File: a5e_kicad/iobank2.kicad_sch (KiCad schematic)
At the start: 2 parts, among them U7 A5EB013B-B23B

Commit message: Add LCSC part numbers and fix C102 footprint
Add a hidden LCSC field to 290 symbols from the JLCPCB parts match
(2026-10-23). Left without LCSC: U7, U15, L1 (not in the JLCPCB
library), C1/C2/C4 and L2-L5 (no value specified), J3 (no confident
match) and Y3 (the 12 pF Basic crystal does not suit the 27 pF load
caps). U2, U12, Y2 and J9 carry the exact-MPN LCSC numbers although
they currently show zero JLCPCB stock.

C102 (22U 6V3) had a 0201 footprint; no 22 uF 0201 part exists. Change
it to 0402 (C415703) like C5-C7.
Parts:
- R24: LCSC (none) -> C25094
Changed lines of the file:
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@@
+			)
+		)
+		(property "LCSC" "C25094"
+			(at 234.95 52.578 90)
+			(hide yes)
+			(show_name no)
+			(do_not_autoplace no)
+			(effects
+				(font
+					(size 1.27 1.27)
+				)
 			)
 		)

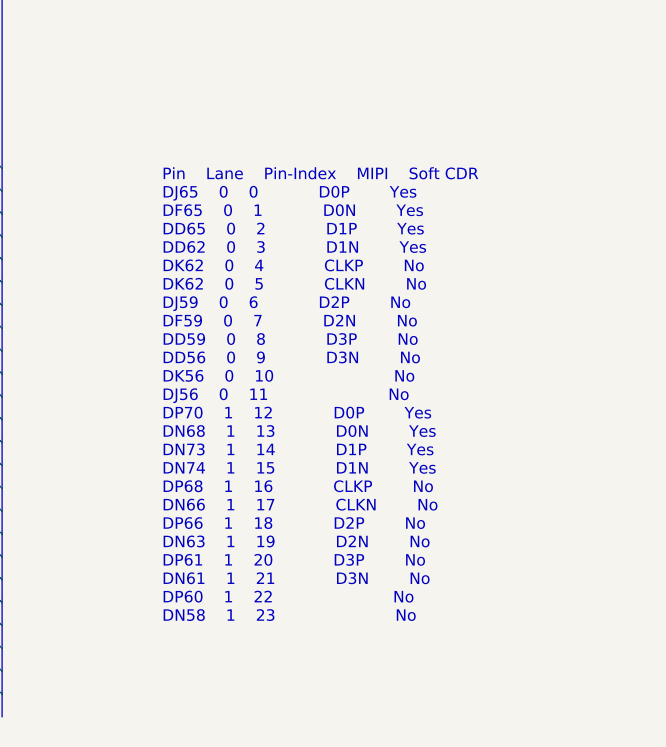
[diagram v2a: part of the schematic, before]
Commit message: Schematic reorg step 1: remove dangling stubs and stale notes, correct notes, fill title blocks
Netlist: 0 renamed, 0 connectivity diffs; DRC parity 0. ERC 315 -> 242.
Plan refreshed for the eMMC, RTL8211FDI, TPS548A28 and the tuned LPDDR4 (IOBANK 3 sheet name kept).
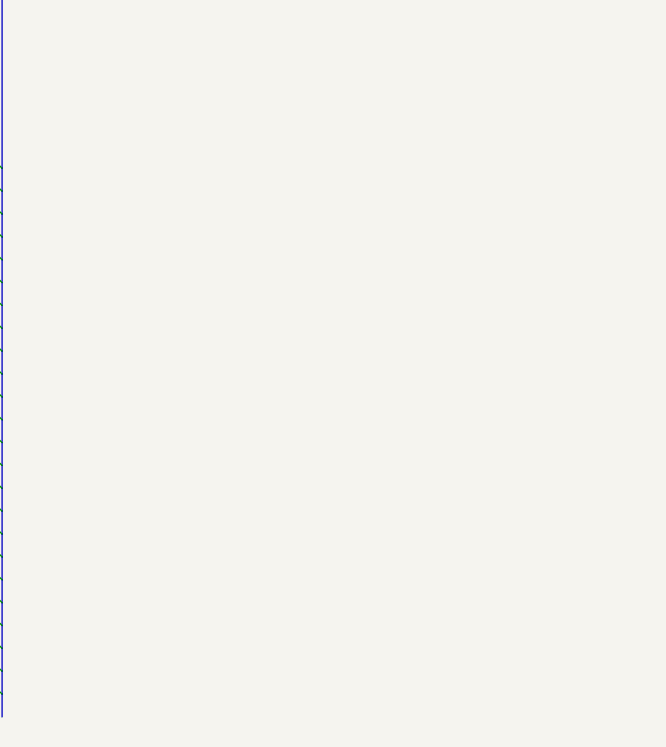
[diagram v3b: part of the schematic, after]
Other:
- note removed: "Pin Lane Pin-Index MIPI Soft CDR DJ65 0 0 D0P Yes DF65 0 1 D0N Yes DD65 0 2 D1P Yes DD62 0 3 D1N Yes DK62 0 4 CLKP No DK62 0 5 CLKN No DJ59 0 6 D2P No DF59 0 7 D2N No DD59 0 8 D3P No DD56 0 9 D3N No DK56 0 10 No DJ56 0 11 No DP70 1 12 D0P Yes DN68 1 13 D0N Yes DN73 1 14 D1P Yes DN74 1 15 D1N Yes DP68 1 16 CLKP No DN66 1 17 CLKN No DP66 1 18 D2P No DN63 1 19 D2N No DP61 1 20 D3P No DN61 1 21 D3N N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"
- title: (none) -> Bank 2A I/O
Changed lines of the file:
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@@
 	(paper "A4")
 	(title_block
-		(rev "0.1")
-	)
-	(text "Pin	Lane	Pin-Index	MIPI	Soft CDR\nDJ65	0	0			D0P		Yes\nDF65	0	1			D0N		Yes\nDD65	0	2			D1P		Yes\nDD62	0	3			D1N		Yes\nDK62	0	4			CLKP		No\nDK62	0	5			CLKN		No\nDJ59	0	6			D2P		No\nDF59	0	7			D2N		No\nDD59	0	8			D3P		No\nDD56	0	9			D3N		No\nDK56	0	10						No\nDJ56	0	11						No\nDP70	1	12			D0P		Yes\nDN68	1	13			D0N		Yes\nDN73	1	14			D1P		Yes\nDN74	1	15			D1N		Yes\nDP68	1	16			CLKP		No\nDN66	1	17			CLKN		No\nDP66	1	18			D2P		No\nDN63	1	19			D2N		No\nDP61	1	20			D3P		No\nDN61	1	21			D3N		No\nDP60	1	22						No\nDN58	1	23						No\n"
-		(exclude_from_sim no)
-		(at 236.22 116.84 0)
-		(effects
-			(font
-				(face "Courier New")
-				(size 1.27 1.27)
-			)
-			(justify left)
-		)
+		(title "Bank 2A I/O")
+		(rev "${REVISION}")
+		(comment 1 "${BOARD}")
 	)
 	(no_connect

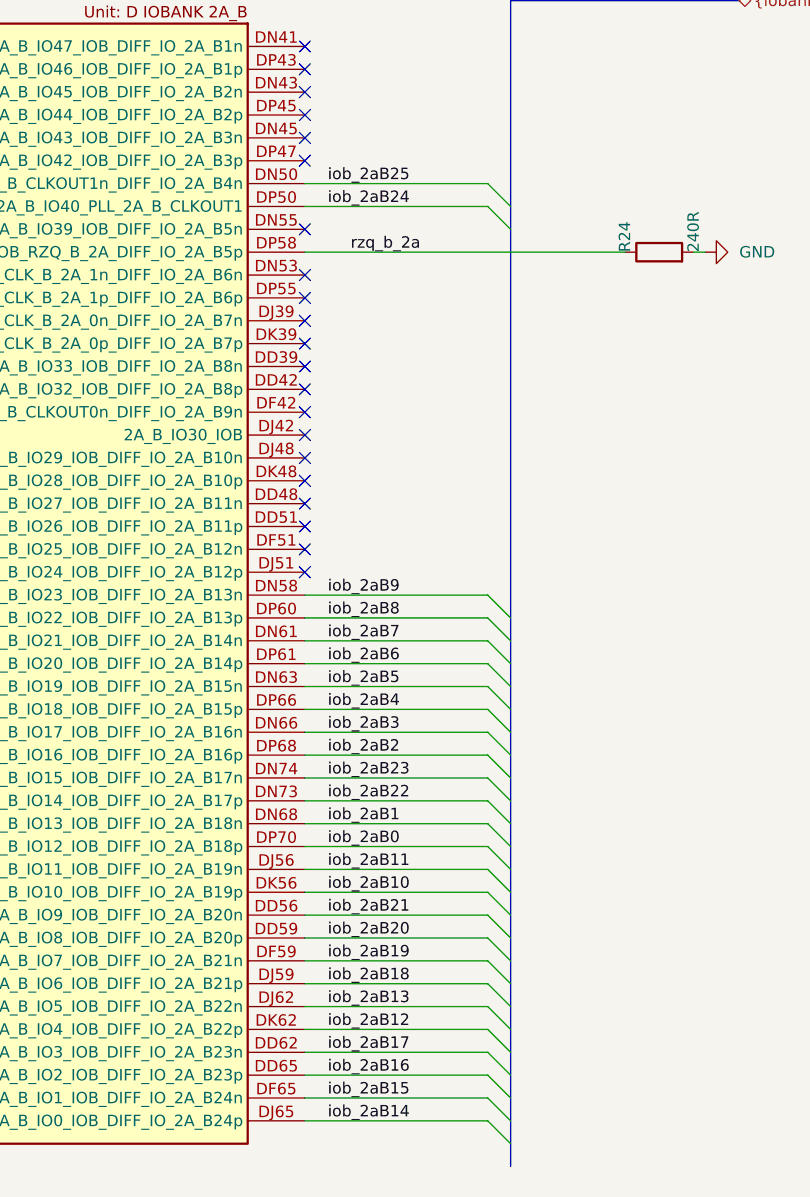
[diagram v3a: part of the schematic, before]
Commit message: Schematic reorg step 7: no global labels, NC flags on unused U7 pins
- hps_uart0_tx/rx, eth_rst_n, phy_rst_n, fpga_led: global labels replaced by
  sheet pins; eth_led_g_n is a local label
- HyperBus labels/bus, the HPS {hps_i2c} bus and the pwr_scl/pwr_sda wiring
  removed (nothing behind them)
- 118 U7 pins that only had a net label: label, stub and bus entry removed,
  no-connect flag added
- Bank 3A notes restacked
- PCB: 124 nets renamed (118 to unconnected-(U7...))

Netdiff: 124 renamed, 0 connectivity diffs. ERC 148 -> 21. DRC parity 0.
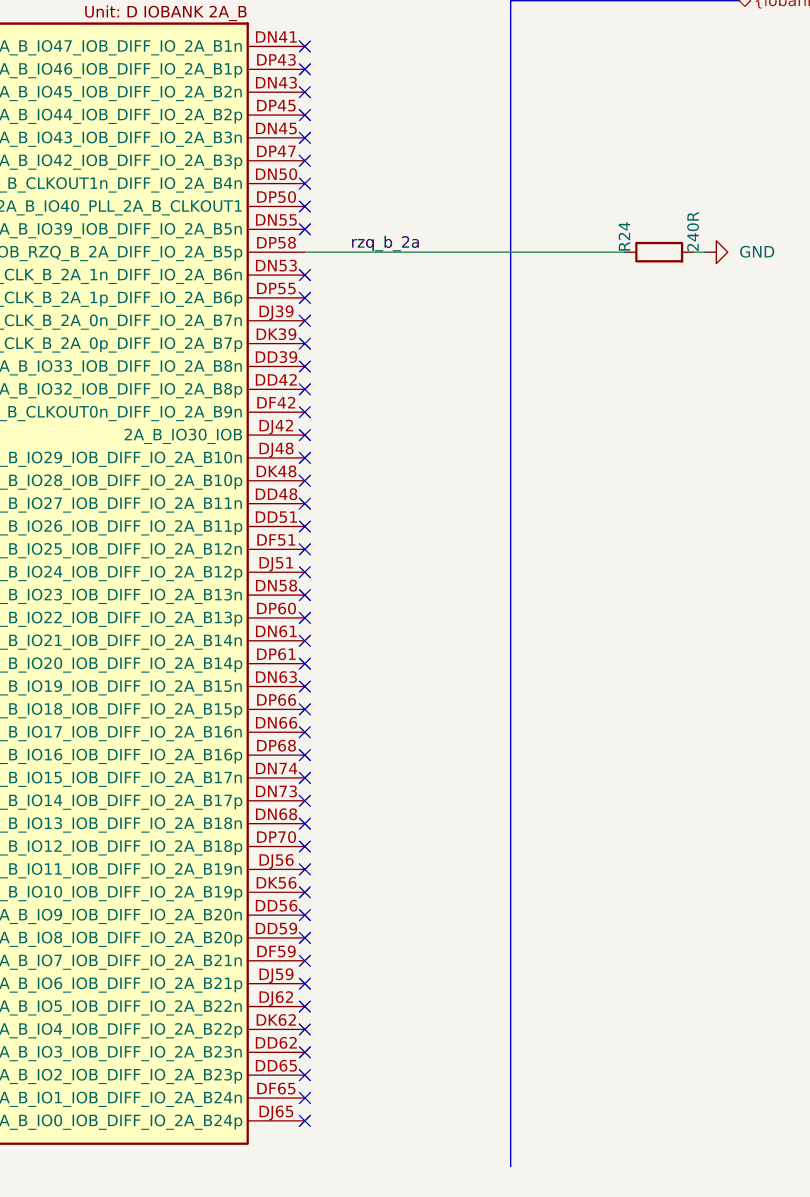
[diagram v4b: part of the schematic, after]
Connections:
- net iob_2aB0: no longer names the net of U7.DP70 (2A_B_IO12_IOB_DIFF_IO_2A_B18p)
- net iob_2aB1: no longer names the net of U7.DN68 (2A_B_IO13_IOB_DIFF_IO_2A_B18n)
- net iob_2aB10: no longer names the net of U7.DK56 (2A_B_IO10_IOB_DIFF_IO_2A_B19p)
- net iob_2aB11: no longer names the net of U7.DJ56 (2A_B_IO11_IOB_DIFF_IO_2A_B19n)
- net iob_2aB12: no longer names the net of U7.DK62 (2A_B_IO4_IOB_DIFF_IO_2A_B22p)
- net iob_2aB13: no longer names the net of U7.DJ62 (2A_B_IO5_IOB_DIFF_IO_2A_B22n)
- net iob_2aB14: no longer names the net of U7.DJ65 (2A_B_IO0_IOB_DIFF_IO_2A_B24p)
- net iob_2aB15: no longer names the net of U7.DF65 (2A_B_IO1_IOB_DIFF_IO_2A_B24n)
- net iob_2aB16: no longer names the net of U7.DD65 (2A_B_IO2_IOB_DIFF_IO_2A_B23p)
- net iob_2aB17: no longer names the net of U7.DD62 (2A_B_IO3_IOB_DIFF_IO_2A_B23n)
- net iob_2aB18: no longer names the net of U7.DJ59 (2A_B_IO6_IOB_DIFF_IO_2A_B21p)
- net iob_2aB19: no longer names the net of U7.DF59 (2A_B_IO7_IOB_DIFF_IO_2A_B21n)
- net iob_2aB2: no longer names the net of U7.DP68 (2A_B_IO16_IOB_DIFF_IO_2A_B16p)
- net iob_2aB20: no longer names the net of U7.DD59 (2A_B_IO8_IOB_DIFF_IO_2A_B20p)
- net iob_2aB21: no longer names the net of U7.DD56 (2A_B_IO9_IOB_DIFF_IO_2A_B20n)
- net iob_2aB22: no longer names the net of U7.DN73 (2A_B_IO14_IOB_DIFF_IO_2A_B17p)
- net iob_2aB23: no longer names the net of U7.DN74 (2A_B_IO15_IOB_DIFF_IO_2A_B17n)
- net iob_2aB24: no longer names the net of U7.DP50 (2A_B_IO40_IOB)
- net iob_2aB25: no longer names the net of U7.DN50 (2A_B_IO41_IOB_PLL_2A_B_CLKOUT1n_DIFF_IO_2A_B4n)
- net iob_2aB3: no longer names the net of U7.DN66 (2A_B_IO17_IOB_DIFF_IO_2A_B16n)
- net iob_2aB4: no longer names the net of U7.DP66 (2A_B_IO18_IOB_DIFF_IO_2A_B15p)
- net iob_2aB5: no longer names the net of U7.DN63 (2A_B_IO19_IOB_DIFF_IO_2A_B15n)
- net iob_2aB6: no longer names the net of U7.DP61 (2A_B_IO20_IOB_DIFF_IO_2A_B14p)
- net iob_2aB7: no longer names the net of U7.DN61 (2A_B_IO21_IOB_DIFF_IO_2A_B14n)
- net iob_2aB8: no longer names the net of U7.DP60 (2A_B_IO22_IOB_DIFF_IO_2A_B13p)
- net iob_2aB9: no longer names the net of U7.DN58 (2A_B_IO23_IOB_DIFF_IO_2A_B13n)
- no-connect marks 69 -> 95
